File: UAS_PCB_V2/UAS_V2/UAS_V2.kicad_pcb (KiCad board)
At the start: 2 copper layers, 50.8 x 50.8 mm, 20 parts, among them J1 UAS_PWR_IN, J10 UAS_SM04B-GHS-TB(LF)(SN)-, J2 UAS_JST-3-pin-Revised-Symbol, J3 UAS_JST-3-pin-Revised-Symbol, J4 UAS_SM07B-GHS-TB(LF)(SN), J5 UAS_SM04B-GHS-TB(LF)(SN)-, J6 UAS_SM04B-GHS-TB(LF)(SN)-, J7 UAS_SM07B-GHS-TB(LF)(SN), J8 UAS_SM08B-GHS-TB(LF)(SN), J9 UAS_SM08B-GHS-TB(LF)(SN)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

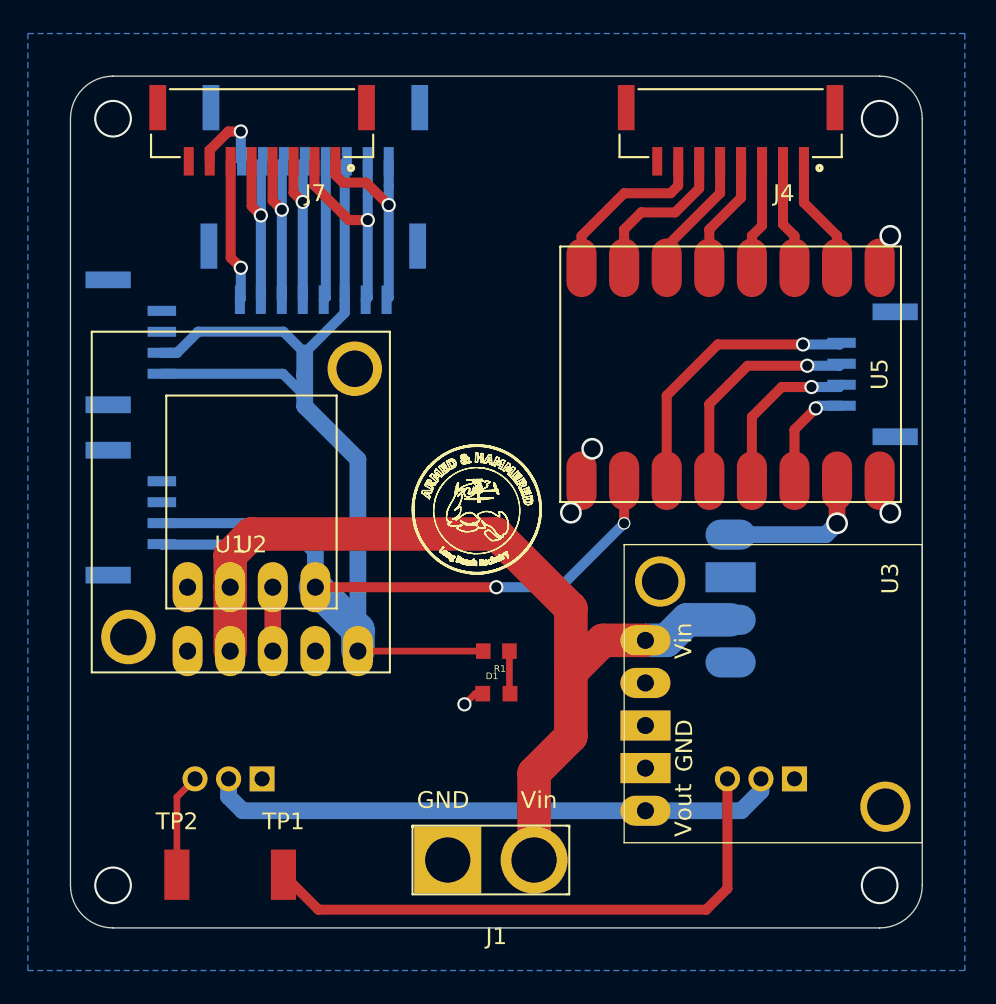
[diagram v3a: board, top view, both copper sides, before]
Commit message: UAS PDP PCB Models
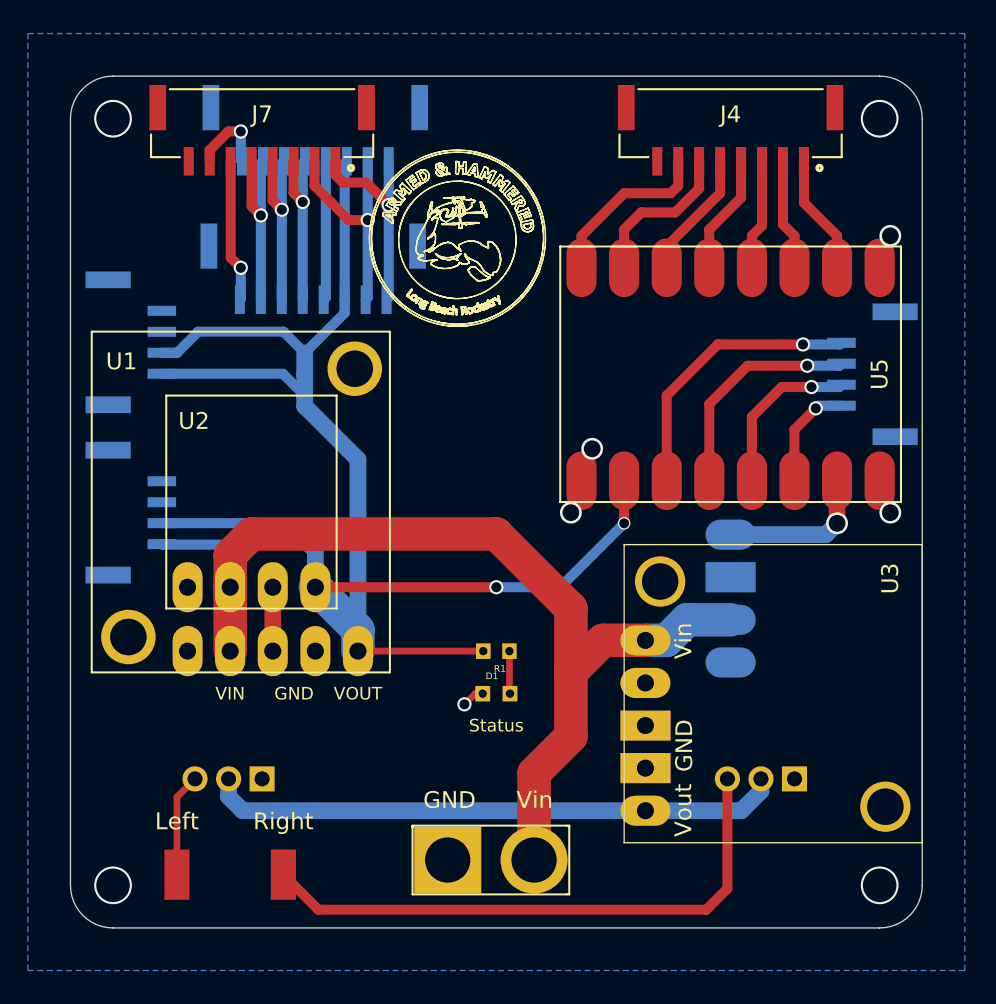
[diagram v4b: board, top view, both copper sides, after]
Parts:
- renumbered TP2 to Left, TP1 to Right
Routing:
- net GND: track 13.5 -> 22.1 mm
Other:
- board text added: "Status"
- board text added: "VIN"
- board text added: "VOUT"
